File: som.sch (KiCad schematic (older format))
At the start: 31 parts, among them M1 SC606T

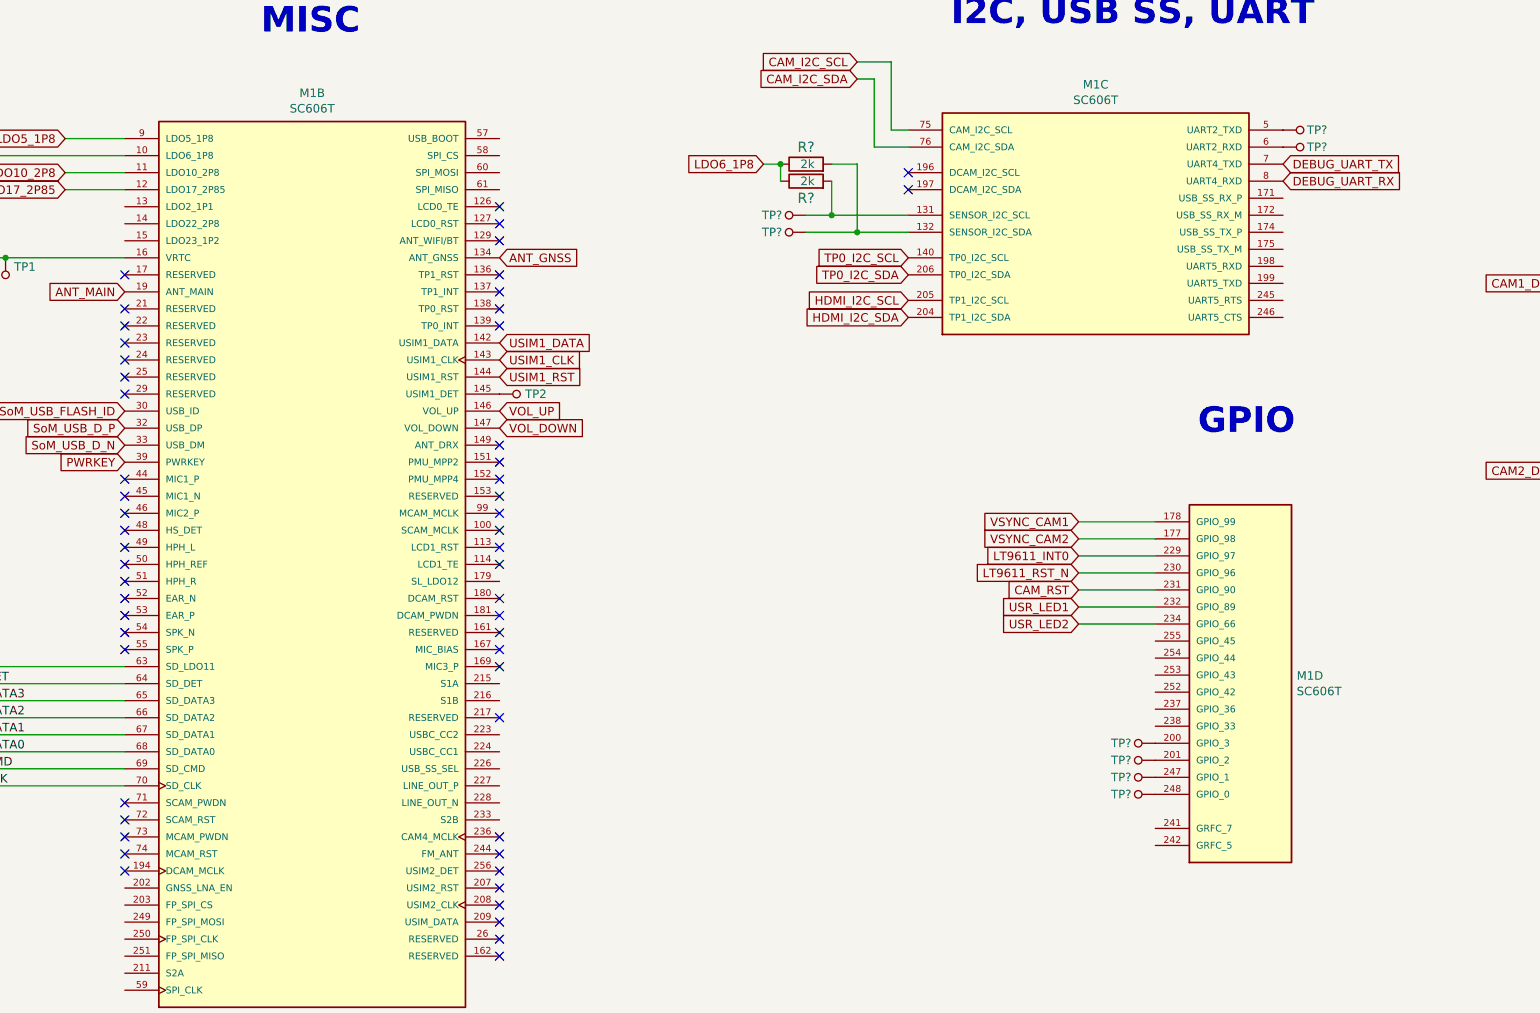
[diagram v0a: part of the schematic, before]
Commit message: Added footprint of 2x USB-A stacked. Added connections to USB HUB.
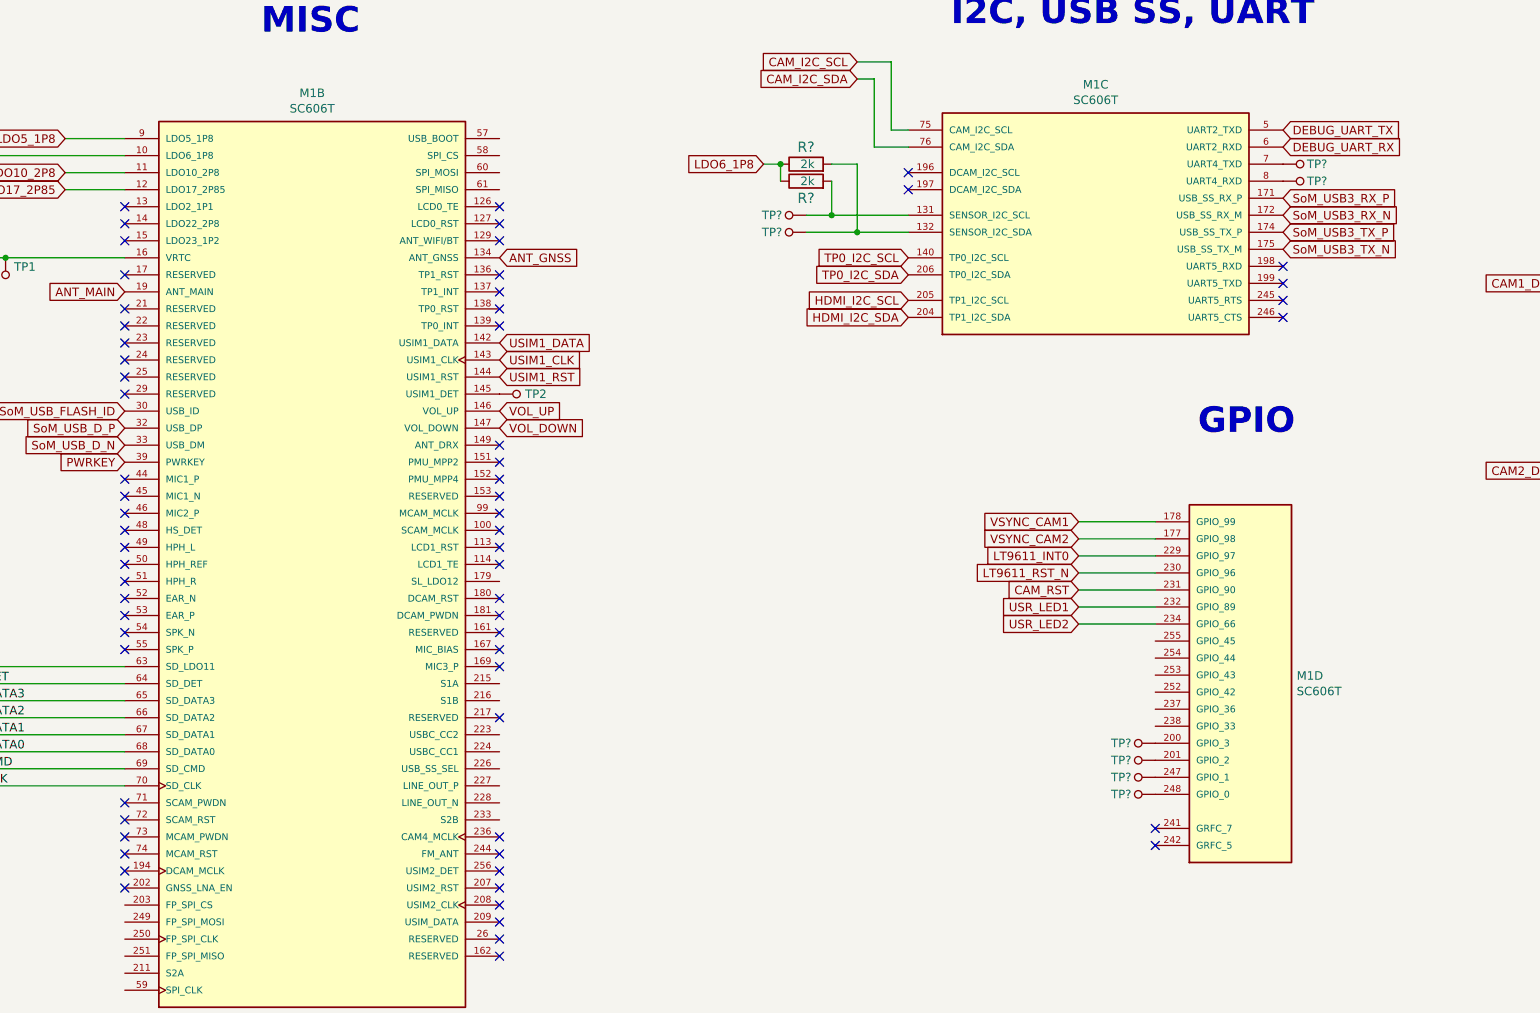
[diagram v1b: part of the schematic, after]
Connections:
- net DEBUG_UART_RX: now also M1.6 (UART2_RXD); no longer M1.8 (UART4_RXD)
- net DEBUG_UART_TX: now also M1.5 (UART2_TXD); no longer M1.7 (UART4_TXD)
- net SoM_USB3_RX_P: now reaches M1.171 (USB_SS_RX_P)
- net SoM_USB3_RX_N: now reaches M1.172 (USB_SS_RX_M)
- net SoM_USB3_TX_P: now reaches M1.174 (USB_SS_TX_P)
- net SoM_USB3_TX_N: now reaches M1.175 (USB_SS_TX_M)
- net at TP?.1: now also M1.7 (UART4_TXD); no longer M1.5 (UART2_TXD)
- net at TP?.1: now also M1.8 (UART4_RXD); no longer M1.6 (UART2_RXD)
- no-connect marks 84 -> 94
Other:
- moved on the sheet: TP?
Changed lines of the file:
@@
 L sc606-baseboard:TP_SMD_0_75MM TP?
 U 1 1 629FCB71
-P 9700 1600
-F 0 "TP?" V 9700 1500 50  0000 C CNN
-F 1 "TP_SMD_0_75MM" H 9700 1500 50  0001 C CNN
-F 2 "sc606-baseboard-footprints:Testpoint_smd_0_75mm" H 9900 1800 60  0001 L CNN
-F 3 "" H 9900 1900 60  0001 L CNN
-	1    9700 1600
+P 9700 1800
+F 0 "TP?" V 9700 1700 50  0000 C CNN
+F 1 "TP_SMD_0_75MM" H 9700 1700 50  0001 C CNN
+F 2 "sc606-baseboard-footprints:Testpoint_smd_0_75mm" H 9900 2000 60  0001 L CNN
+F 3 "" H 9900 2100 60  0001 L CNN
+	1    9700 1800
 	0    -1   -1   0
 $EndComp
@@
 L sc606-baseboard:TP_SMD_0_75MM TP?
 U 1 1 629FCB77
-P 9700 1700
-F 0 "TP?" V 9700 1600 50  0000 C CNN
-F 1 "TP_SMD_0_75MM" H 9700 1600 50  0001 C CNN
-F 2 "sc606-baseboard-footprints:Testpoint_smd_0_75mm" H 9900 1900 60  0001 L CNN
-F 3 "" H 9900 2000 60  0001 L CNN
-	1    9700 1700
+P 9700 1900
+F 0 "TP?" V 9700 1800 50  0000 C CNN
+F 1 "TP_SMD_0_75MM" H 9700 1800 50  0001 C CNN
+F 2 "sc606-baseboard-footprints:Testpoint_smd_0_75mm" H 9900 2100 60  0001 L CNN
+F 3 "" H 9900 2200 60  0001 L CNN
+	1    9700 1900
 	0    -1   -1   0
 $EndComp
 Text GLabel 2800 3250 0    50   Input ~ 0
 SoM_USB_FLASH_ID
-Text GLabel 9600 1900 2    50   Input ~ 0
+Text GLabel 9600 1700 2    50   Input ~ 0
 DEBUG_UART_RX
-Text GLabel 9600 1800 2    50   Input ~ 0
+Text GLabel 9600 1600 2    50   Input ~ 0
 DEBUG_UART_TX
+Text GLabel 9600 2200 2    50   Input ~ 0
+SoM_USB3_TX_P
+Text GLabel 9600 2300 2    50   Input ~ 0
+SoM_USB3_TX_N
+Text GLabel 9600 2000 2    50   Input ~ 0
+SoM_USB3_RX_P
+Text GLabel 9600 2100 2    50   Input ~ 0
+SoM_USB3_RX_N
+NoConn ~ 9600 2400
+NoConn ~ 9600 2500
+NoConn ~ 9600 2600
+NoConn ~ 9600 2700
+NoConn ~ 2800 6050
+NoConn ~ 8850 5700
+NoConn ~ 8850 5800
+NoConn ~ 2800 2050
+NoConn ~ 2800 2150
+NoConn ~ 2800 2250
 Wire Bus Line
 	1750 4650 1750 5350
